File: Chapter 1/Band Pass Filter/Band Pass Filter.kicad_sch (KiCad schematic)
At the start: 4 parts

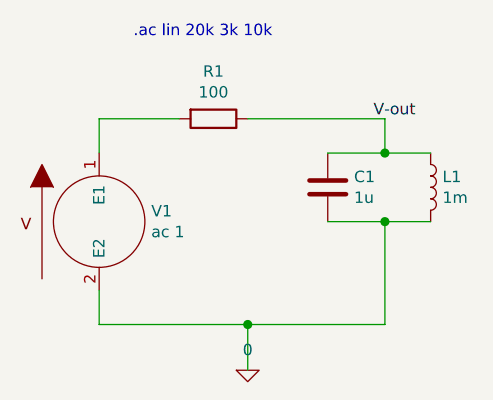
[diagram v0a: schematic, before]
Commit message: added v out tags to Chapter 1
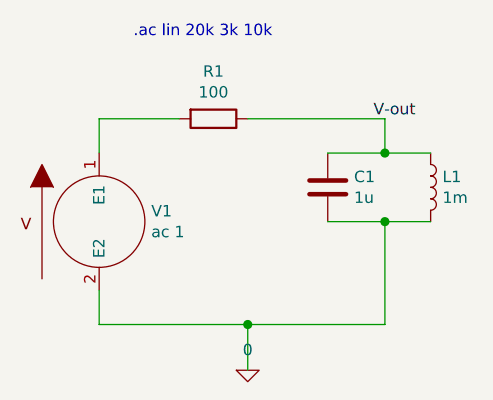
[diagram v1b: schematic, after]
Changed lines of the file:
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@@
-(kicad_sch (version 20210406) (generator eeschema)
+(kicad_sch (version 20211123) (generator eeschema)
   (paper "A4")
-  (junction (at 101.6 58.42) (diameter 1.016) (color 0 0 0 0))
-  (junction (at 116.84 39.37) (diameter 1.016) (color 0 0 0 0))
-  (junction (at 116.84 46.99) (diameter 1.016) (color 0 0 0 0))
+  (junction (at 116.84 39.37) (diameter 1.016) (color 0 0 0 0)
+  )
+  (junction (at 116.84 46.99) (diameter 1.016) (color 0 0 0 0)
+  )
+  (junction (at 101.6 58.42) (diameter 1.016) (color 0 0 0 0)
+  )
+  (wire (pts (xy 116.84 39.37) (xy 110.49 39.37))
+    (stroke (width 0) (type solid) (color 0 0 0 0))
+  )
+  (wire (pts (xy 93.98 35.56) (xy 85.09 35.56))
+    (stroke (width 0) (type solid) (color 0 0 0 0))
+  )
+  (wire (pts (xy 121.92 39.37) (xy 116.84 39.37))
+    (stroke (width 0) (type solid) (color 0 0 0 0))
+  )
   (wire (pts (xy 85.09 35.56) (xy 85.09 39.37))
+    (stroke (width 0) (type solid) (color 0 0 0 0))
+  )
+  (wire (pts (xy 116.84 58.42) (xy 116.84 46.99))
+    (stroke (width 0) (type solid) (color 0 0 0 0))
+  )
+  (wire (pts (xy 116.84 35.56) (xy 101.6 35.56))
+    (stroke (width 0) (type solid) (color 0 0 0 0))
+  )
+  (wire (pts (xy 116.84 46.99) (xy 121.92 46.99))
+    (stroke (width 0) (type solid) (color 0 0 0 0))
+  )
+  (wire (pts (xy 101.6 63.5) (xy 101.6 58.42))
+    (stroke (width 0) (type solid) (color 0 0 0 0))
+  )
+  (wire (pts (xy 101.6 58.42) (xy 116.84 58.42))
+    (stroke (width 0) (type solid) (color 0 0 0 0))
+  )
+  (wire (pts (xy 85.09 58.42) (xy 101.6 58.42))
+    (stroke (width 0) (type solid) (color 0 0 0 0))
+  )
+  (wire (pts (xy 110.49 46.99) (xy 116.84 46.99))
     (stroke (width 0) (type solid) (color 0 0 0 0))
   )
@@
     (stroke (width 0) (type solid) (color 0 0 0 0))
   )
-  (wire (pts (xy 85.09 58.42) (xy 101.6 58.42))
-    (stroke (width 0) (type solid) (color 0 0 0 0))
-  )
-  (wire (pts (xy 93.98 35.56) (xy 85.09 35.56))
-    (stroke (width 0) (type solid) (color 0 0 0 0))
-  )
-  (wire (pts (xy 101.6 58.42) (xy 116.84 58.42))
-    (stroke (width 0) (type solid) (color 0 0 0 0))
-  )
-  (wire (pts (xy 101.6 63.5) (xy 101.6 58.42))
-    (stroke (width 0) (type solid) (color 0 0 0 0))
-  )
-  (wire (pts (xy 110.49 46.99) (xy 116.84 46.99))
-    (stroke (width 0) (type solid) (color 0 0 0 0))
-  )
-  (wire (pts (xy 116.84 35.56) (xy 101.6 35.56))
-    (stroke (width 0) (type solid) (color 0 0 0 0))
-  )
-  (wire (pts (xy 116.84 39.37) (xy 110.49 39.37))
-    (stroke (width 0) (type solid) (color 0 0 0 0))
-  )
   (wire (pts (xy 116.84 39.37) (xy 116.84 35.56))
-    (stroke (width 0) (type solid) (color 0 0 0 0))
-  )
-  (wire (pts (xy 116.84 46.99) (xy 121.92 46.99))
-    (stroke (width 0) (type solid) (color 0 0 0 0))
-  )
-  (wire (pts (xy 116.84 58.42) (xy 116.84 46.99))
-    (stroke (width 0) (type solid) (color 0 0 0 0))
-  )
-  (wire (pts (xy 121.92 39.37) (xy 116.84 39.37))
     (stroke (width 0) (type solid) (color 0 0 0 0))
   )
@@
     (effects (font (size 1.27 1.27)) (justify left bottom))
   )
-  (symbol (lib_id "Band-Pass-Filter-rescue:0-pspice") (at 101.6 63.5 0) (unit 1)
+  (symbol (lib_id "Band-Pass-Filter-rescue:VSOURCE-pspice") (at 85.09 46.99 0) (unit 1)
     (in_bom yes) (on_board yes)
-    (property "Reference" "#GND01" (id 0) (at 101.6 66.04 0)
+    (property "Reference" "V1" (id 0) (at 90.8812 45.8216 0)
+      (effects (font (size 1.27 1.27)) (justify left))
+    )
+    (property "Value" "ac 1" (id 1) (at 90.8812 48.133 0)
+      (effects (font (size 1.27 1.27)) (justify left))
+    )
+    (property "Footprint" "" (id 2) (at 85.09 46.99 0)
       (effects (font (size 1.27 1.27)) hide)
     )
-    (property "Value" "0" (id 1) (at 101.6 61.2394 0))
-    (property "Footprint" "" (id 2) (at 101.6 63.5 0)
-      (effects (font (size 1.27 1.27)) hide)
-    )
-    (property "Datasheet" "~" (id 3) (at 101.6 63.5 0)
-      (effects (font (size 1.27 1.27)) hide)
-    )
-    (pin "1")
-  )
-  (symbol (lib_id "Band-Pass-Filter-rescue:L-Device") (at 121.92 43.18 0) (unit 1)
-    (in_bom yes) (on_board yes)
-    (property "Reference" "L1" (id 0) (at 123.2408 42.0116 0)
-      (effects (font (size 1.27 1.27)) (justify left))
-    )
-    (property "Value" "1m" (id 1) (at 123.2408 44.323 0)
-      (effects (font (size 1.27 1.27)) (justify left))
-    )
-    (property "Footprint" "" (id 2) (at 121.92 43.18 0)
-      (effects (font (size 1.27 1.27)) hide)
-    )
-    (property "Datasheet" "~" (id 3) (at 121.92 43.18 0)
+    (property "Datasheet" "~" (id 3) (at 85.09 46.99 0)
       (effects (font (size 1.27 1.27)) hide)
     )
@@
     (pin "2")
   )
-  (symbol (lib_id "Band-Pass-Filter-rescue:VSOURCE-pspice") (at 85.09 46.99 0) (unit 1)
+  (symbol (lib_id "Band-Pass-Filter-rescue:L-Device") (at 121.92 43.18 0) (unit 1)
     (in_bom yes) (on_board yes)
-    (property "Reference" "V1" (id 0) (at 90.8812 45.8216 0)
+    (property "Reference" "L1" (id 0) (at 123.2408 42.0116 0)
       (effects (font (size 1.27 1.27)) (justify left))
     )
-    (property "Value" "ac 1" (id 1) (at 90.8812 48.133 0)
+    (property "Value" "1m" (id 1) (at 123.2408 44.323 0)
       (effects (font (size 1.27 1.27)) (justify left))
     )
-    (property "Footprint" "" (id 2) (at 85.09 46.99 0)
+    (property "Footprint" "" (id 2) (at 121.92 43.18 0)
       (effects (font (size 1.27 1.27)) hide)
     )
-    (property "Datasheet" "~" (id 3) (at 85.09 46.99 0)
+    (property "Datasheet" "~" (id 3) (at 121.92 43.18 0)
       (effects (font (size 1.27 1.27)) hide)
     )
@@
     (pin "2")
   )
+  (symbol (lib_id "Band-Pass-Filter-rescue:0-pspice") (at 101.6 63.5 0) (unit 1)
+    (in_bom yes) (on_board yes)
+    (property "Reference" "#GND01" (id 0) (at 101.6 66.04 0)
+      (effects (font (size 1.27 1.27)) hide)
+    )
+    (property "Value" "0" (id 1) (at 101.6 61.2394 0))
+    (property "Footprint" "" (id 2) (at 101.6 63.5 0)
+      (effects (font (size 1.27 1.27)) hide)
+    )
+    (property "Datasheet" "~" (id 3) (at 101.6 63.5 0)
+      (effects (font (size 1.27 1.27)) hide)
+    )
+    (pin "1")
+  )
   (sheet_instances
